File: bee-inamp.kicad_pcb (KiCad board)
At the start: 2 copper layers, 13.7 x 53.3 mm, 25 parts, among them J1 Conn_01x02_Male, J2 Conn_01x02_Male, J3 Conn_01x02_Male, J4 Conn_01x02_Male, J5 Conn_01x02, J6 Conn_01x02, J7 Conn_02x03_Odd_Even, J8 Conn_01x03, J9 Conn_01x02, U1 INA126

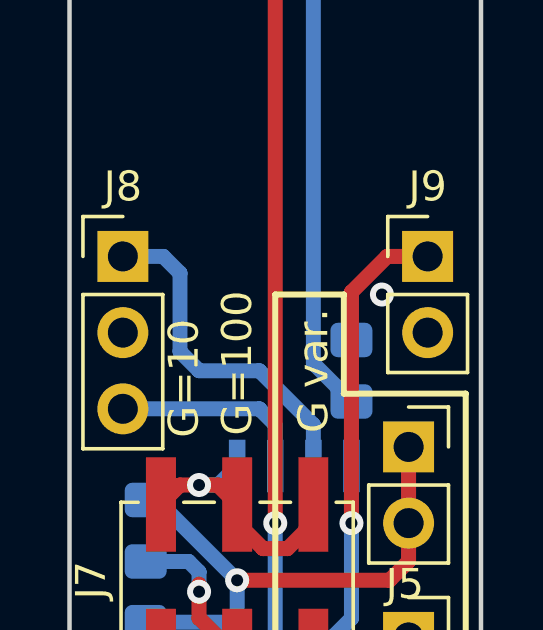
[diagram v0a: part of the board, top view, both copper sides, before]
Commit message: DRC - remove unnecessary via.
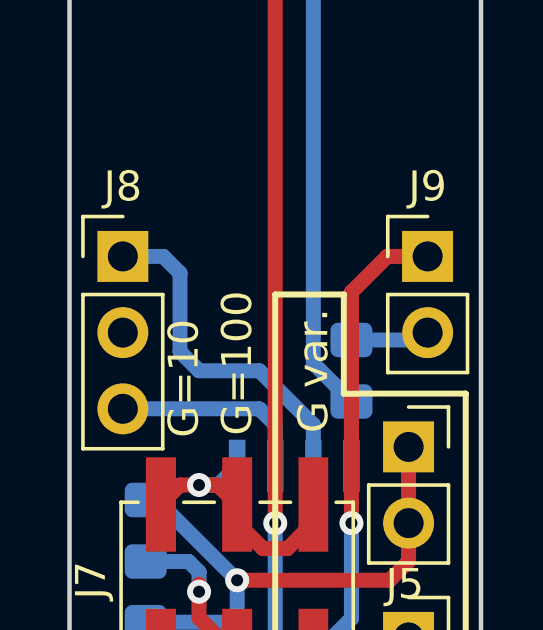
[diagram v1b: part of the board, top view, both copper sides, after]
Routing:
- net GND: track 0.00 -> 2.64 mm, vias 1 -> 0
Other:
- net class Default: trace_width 0.25 -> 0.5
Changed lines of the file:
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@@
     (thickness 1.6)
     (drawings 13)
-    (tracks 87)
+    (tracks 88)
     (zones 0)
     (modules 25)
@@
   )
   (setup
-    (last_trace_width 0.25)
+    (last_trace_width 0.5)
     (user_trace_width 0.5)
     (trace_clearance 0.2)
@@
   (net_class Default "Dies ist die voreingestellte Netzklasse."
     (clearance 0.2)
-    (trace_width 0.25)
+    (trace_width 0.5)
     (via_dia 0.8)
     (via_drill 0.4)
@@
   (segment (start 81.910002 91.44) (end 78.74 91.44) (width 0.5) (layer F.Cu) (net 2))
   (segment (start 82.190001 91.719999) (end 81.910002 91.44) (width 0.5) (layer F.Cu) (net 2))
-  (via (at 84.836 114.3) (size 0.8) (drill 0.4) (layers F.Cu B.Cu) (net 3))
+  (segment (start 86.115 115.815) (end 86.36 115.57) (width 0.5) (layer B.Cu) (net 3))
+  (segment (start 83.82 115.815) (end 86.115 115.815) (width 0.5) (layer B.Cu) (net 3))
   (segment (start 78.74 137.16) (end 83.82 137.16) (width 0.5) (layer F.Cu) (net 4))
   (segment (start 85.725 119.38) (end 85.725 121.92) (width 0.5) (layer F.Cu) (net 5))

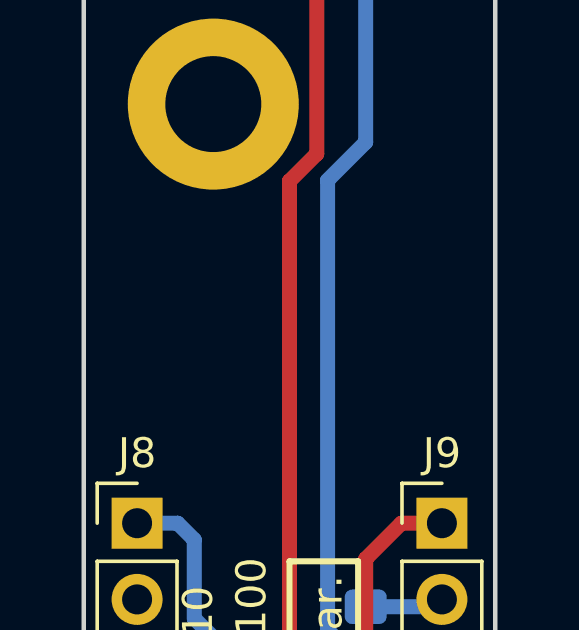
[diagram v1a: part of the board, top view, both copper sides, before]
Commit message: Add text and logos.
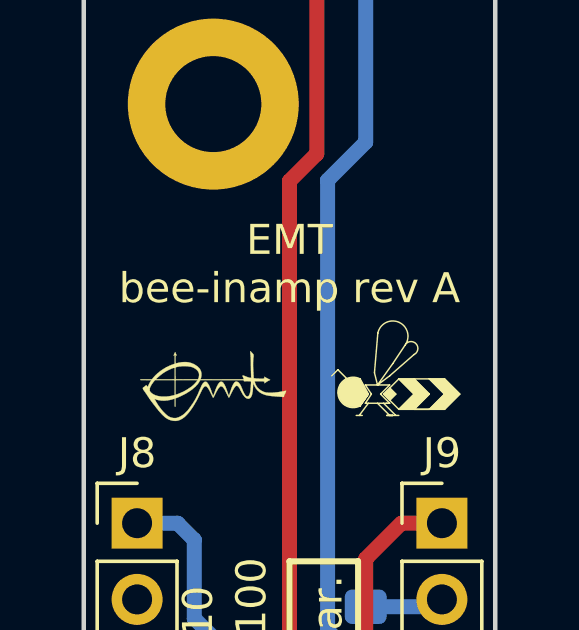
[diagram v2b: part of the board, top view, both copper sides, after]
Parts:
- added H11: Silkscreen_Label, Symbol-emt:EMT-Logo_5.1x2.5mm_Silkscreen, F.Cu at (78.7, 108.5)
- added H12: Silkscreen_Label, Symbol-emt:BEE-Logo_Silkscreen_small, F.Cu at (84.6, 108.7)
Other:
- board text added: "EMT bee-inamp rev A"

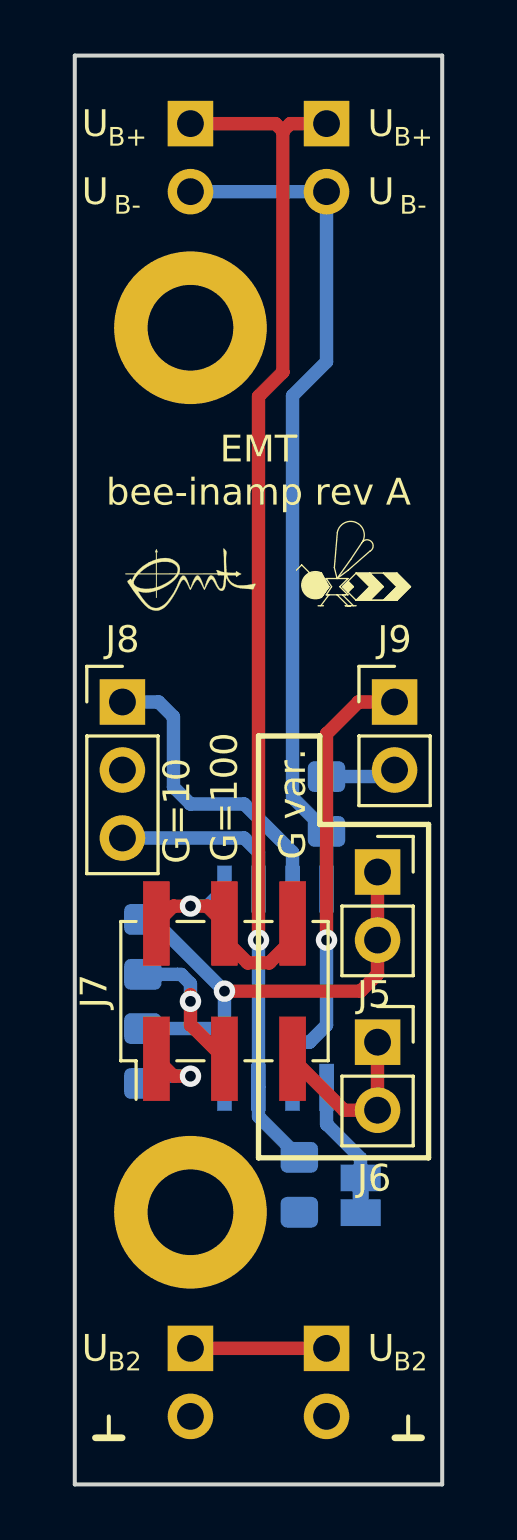
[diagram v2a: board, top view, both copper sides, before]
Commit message: Replace SO package by SOIC. Fixes #1.
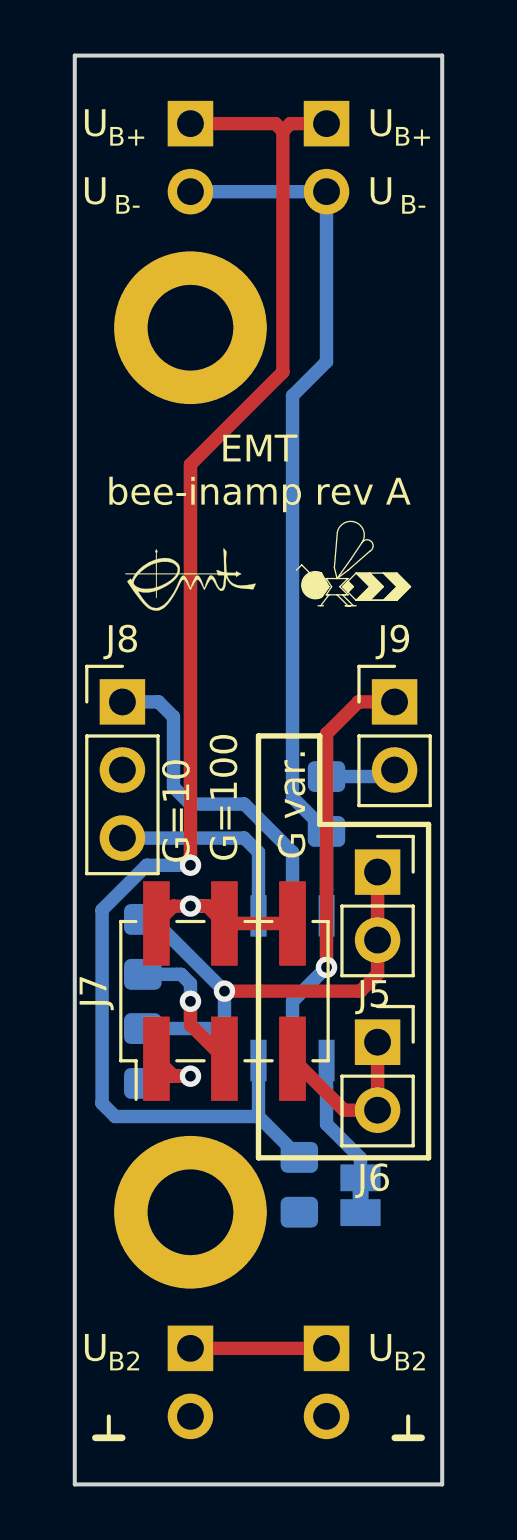
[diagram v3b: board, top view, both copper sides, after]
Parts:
- R2: value 820R -> 820
- U1: footprint Package_SO:SO-8_5.3x6.2mm_P1.27mm -> Package_SO:SOIC-8_3.9x4.9mm_P1.27mm
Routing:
- net +15V: track 44.6 -> 55.7 mm
- net Net-(J9-Pad1): track 16.9 -> 15.8 mm
- net in-: track 6.67 -> 7.67 mm
- net in+: track 11.6 -> 12.6 mm
- net Rg_2: track 20.6 -> 19.6 mm
- net Net-(JP1-Pad1): track 3.91 -> 4.91 mm
- net -15V: track 32.2 -> 33.2 mm
- net Rg_1: track 9.11 -> 8.29 mm

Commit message: Relabel as bee specific.
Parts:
- H1, H2: footprint Symbol-emt:Text_U_B+_Silkscreen -> Symbol-bee:Text_U_B+_Silkscreen
- H11: footprint Symbol-emt:EMT-Logo_5.1x2.5mm_Silkscreen -> Symbol-bee:EMT-Logo_5.1x2.5mm_Silkscreen
- H12: footprint Symbol-emt:BEE-Logo_Silkscreen_small -> Symbol-bee:BEE-Logo_Silkscreen_small
- H3, H4: footprint Symbol-emt:Text_U_B-_Silkscreen -> Symbol-bee:Text_U_B-_Silkscreen
- H5, H6: footprint Symbol-emt:Text_U_B2_Silkscreen -> Symbol-bee:Text_U_B2_Silkscreen
- H7, H8: footprint Symbol-emt:Symbol_GND_Silkscreen -> Symbol-bee:Symbol_GND_Silkscreen
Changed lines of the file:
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@@
     )
   )
-  (module Symbol-emt:Text_U_B+_Silkscreen (layer F.Cu)
+  (module Symbol-bee:Text_U_B+_Silkscreen (layer F.Cu)
     (at 75.184 91.44)
     (descr "Voltage Label Betriebsspannung")
@@
     )
   )
-  (module Symbol-emt:Text_U_B+_Silkscreen (layer F.Cu)
+  (module Symbol-bee:Text_U_B+_Silkscreen (layer F.Cu)
     (at 85.852 91.44)
     (descr "Voltage Label Betriebsspannung")
@@
     )
   )
-  (module Symbol-emt:Text_U_B-_Silkscreen (layer F.Cu)
+  (module Symbol-bee:Text_U_B-_Silkscreen (layer F.Cu)
     (at 75.184 93.98)
     (descr "Voltage Label Betriebsspannung")
@@
     )
   )
-  (module Symbol-emt:Text_U_B-_Silkscreen (layer F.Cu)
+  (module Symbol-bee:Text_U_B-_Silkscreen (layer F.Cu)
     (at 85.852 93.98)
     (descr "Voltage Label Betriebsspannung")
@@
     )
   )
-  (module Symbol-emt:Text_U_B2_Silkscreen (layer F.Cu)
+  (module Symbol-bee:Text_U_B2_Silkscreen (layer F.Cu)
     (at 75.184 137.16)
     (descr "Voltage Label Betriebsspannung")
@@
     )
   )
-  (module Symbol-emt:Text_U_B2_Silkscreen (layer F.Cu)
+  (module Symbol-bee:Text_U_B2_Silkscreen (layer F.Cu)
     (at 85.852 137.16)
     (descr "Voltage Label Betriebsspannung")
@@
     )
   )
-  (module Symbol-emt:Symbol_GND_Silkscreen (layer F.Cu)
+  (module Symbol-bee:Symbol_GND_Silkscreen (layer F.Cu)
     (at 75.692 139.7)
     (descr "Symbol GND")
@@
     (fp_line (start -0.5 0.8) (end 0.5 0.8) (layer F.SilkS) (width 0.25))
   )
-  (module Symbol-emt:Symbol_GND_Silkscreen (layer F.Cu)
+  (module Symbol-bee:Symbol_GND_Silkscreen (layer F.Cu)
     (at 86.868 139.7)
     (descr "Symbol GND")
@@
       (net 3 GND))
   )
-  (module Symbol-emt:EMT-Logo_5.1x2.5mm_Silkscreen (layer F.Cu)
+  (module Symbol-bee:EMT-Logo_5.1x2.5mm_Silkscreen (layer F.Cu)
     (at 78.74 108.458)
     (descr EMT-Logo)
@@
       (xy 1.243014 -1.158797)) (layer F.SilkS) (width 0.01))
   )
-  (module Symbol-emt:BEE-Logo_Silkscreen_small (layer F.Cu)
+  (module Symbol-bee:BEE-Logo_Silkscreen_small (layer F.Cu)
     (at 84.582 108.712)
     (descr BEE-Logo)
